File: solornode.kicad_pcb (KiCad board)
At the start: 2 copper layers, 35.9 x 42.4 mm, 77 parts, among them J1 Conn_01x06, Q1 Q_NMOS_GDS, Q4 Q_PNP_BCE, Q5 Q_NPN_BCE, SW1 SW_Push, U1 LM358, U2 OC5864, U3 PY32F003F1xUx, U4 MAX485E, U5 SGM2033-5.0

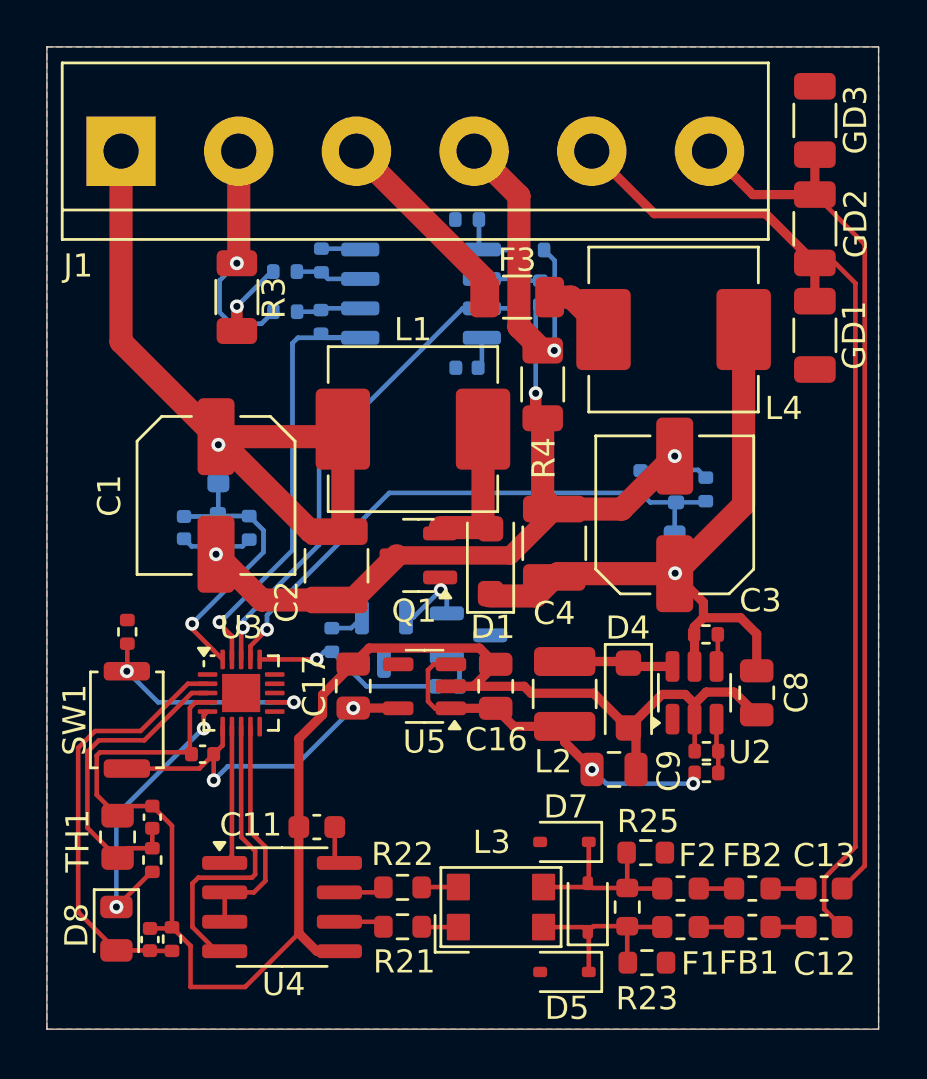
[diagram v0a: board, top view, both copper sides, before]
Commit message: 添加GPIO引出接口和一个LED
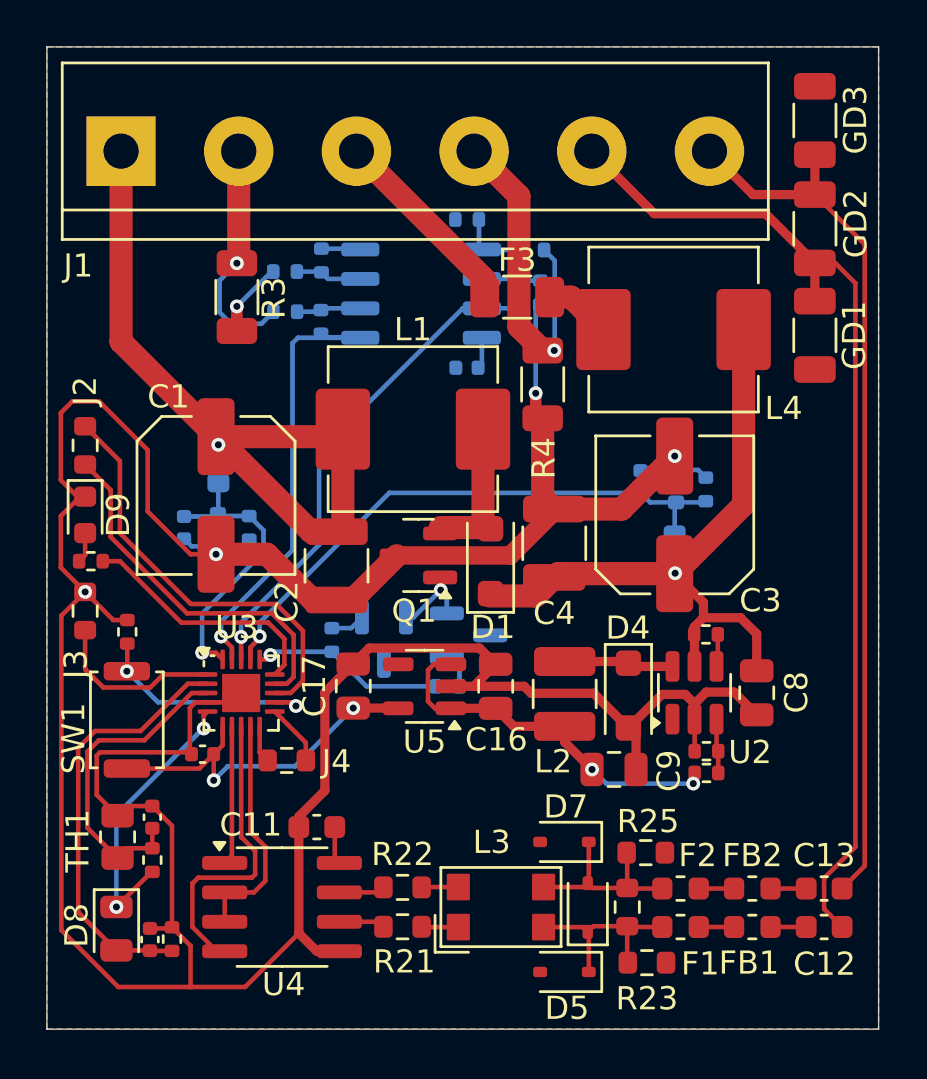
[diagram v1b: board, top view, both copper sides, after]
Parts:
- added D9: LED, LED_SMD:LED_0603_1608Metric, F.Cu at (114.2, 77.1)
- added J2: Conn_01x02, Resistor_SMD:R_0603_1608Metric, F.Cu at (114.2, 74.1)
- added J3: Conn_01x02, Resistor_SMD:R_0603_1608Metric, F.Cu at (114.2, 81.2)
- added J4: Conn_01x02, Resistor_SMD:R_0603_1608Metric, F.Cu at (123.0, 87.7)
- added R28: 470, Resistor_SMD:R_0402_1005Metric, F.Cu at (114.5, 79.1)
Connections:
- U3 pad 1: unconnected-(U3-PA5-Pad1) -> Net-(J3-Pin_1)
- U3 pad 13: unconnected-(U3-OSCIN_PF0-Pad13) -> Net-(J2-Pin_1)
- U3 pad 14: unconnected-(U3-OSCOUT_PF1-Pad14) -> Net-(J2-Pin_2)
- U3 pad 15: unconnected-(U3-NRST_PF2-Pad15) -> Net-(U3-NRST_PF2)
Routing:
- net GND: track 104.6 -> 150.9 mm, vias 2 -> 3
- net Net-(J2-Pin_1): track 0.00 -> 18.5 mm
- net Net-(J2-Pin_2): track 0.00 -> 16.0 mm
- net Net-(U3-NRST_PF2): track 0.00 -> 10.9 mm
- net Net-(J3-Pin_1): track 0.00 -> 7.53 mm
- net /I2C_SDA: track 0.00 -> 2.67 mm
- net /I2C_SCL: track 0.00 -> 1.60 mm
- net Net-(D9-A): track 0.00 -> 1.32 mm

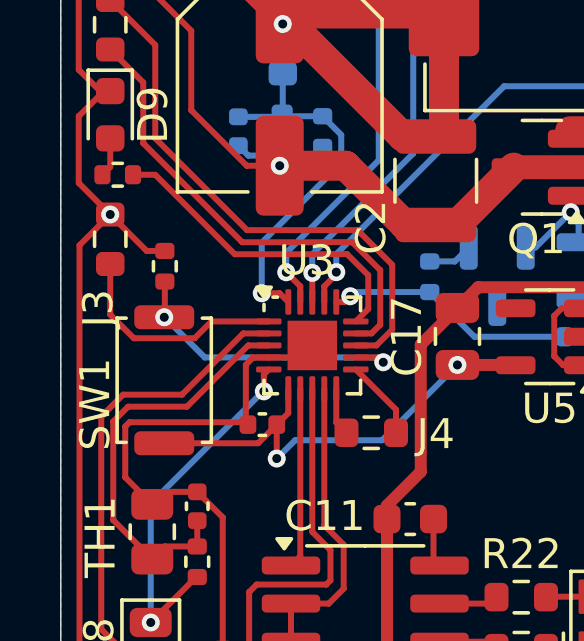
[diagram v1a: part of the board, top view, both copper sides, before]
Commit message: 微调布局和丝印位置
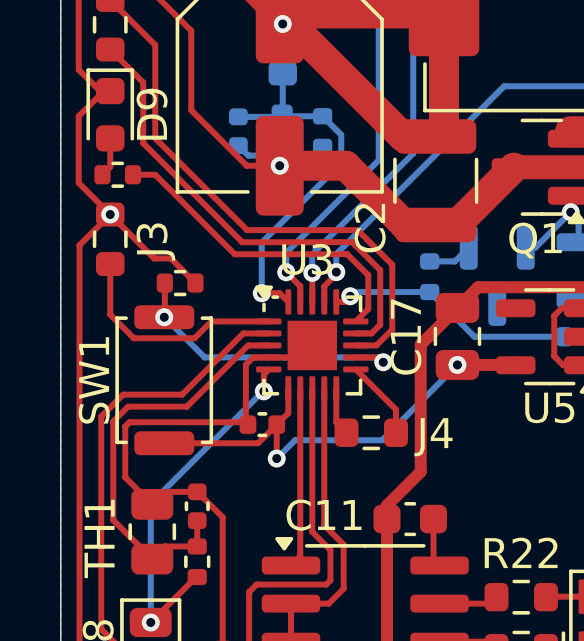
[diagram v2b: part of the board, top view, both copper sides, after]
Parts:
- moved R20 0.76 mm to (116.6, 82.7), turned to 0 degrees
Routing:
- net GND: track 150.9 -> 152.4 mm
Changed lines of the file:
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@@
 	(footprint "Resistor_SMD:R_0402_1005Metric"
 		(layer "F.Cu")
-		(at 116.07 82.15 90)
+		(at 116.58 82.71)
 		(descr "Resistor SMD 0402 (1005 Metric), square (rectangular) end terminal, IPC_7351 nominal, (Body size source: IPC-SM-782 page 72, https://www.pcb-3d.com/wordpress/wp-content/uploads/ipc-sm-782a_amendment_1_and_2.pdf), generated with kicad-footprint-generator")
 		(tags "resistor")
 		(property "Reference" "R20"
-			(at 0 -1.17 90)
+			(at 0 -1.17 360)
 			(layer "F.SilkS")
 			(hide yes)
@@
 		)
 		(property "Value" "R"
-			(at 0 1.17 90)
+			(at 0 1.17 360)
 			(layer "F.Fab")
 			(effects
@@
 		)
 		(property "Footprint" "Resistor_SMD:R_0402_1005Metric"
-			(at 0 0 90)
+			(at 0 0 0)
 			(unlocked yes)
 			(layer "F.Fab")
@@
 		)
 		(property "Datasheet" ""
-			(at 0 0 90)
+			(at 0 0 0)
 			(unlocked yes)
 			(layer "F.Fab")
@@
 		)
 		(property "Description" "Resistor"
-			(at 0 0 90)
+			(at 0 0 0)
 			(unlocked yes)
 			(layer "F.Fab")
@@
 		)
 		(fp_line
-			(start 0.93 -0.47)
-			(end 0.93 0.47)
+			(start -0.93 -0.47)
+			(end 0.93 -0.47)
 			(stroke
 				(width 0.05)
@@
 		)
 		(fp_line
-			(start -0.93 -0.47)
-			(end 0.93 -0.47)
+			(start -0.93 0.47)
+			(end -0.93 -0.47)
 			(stroke
 				(width 0.05)
@@
 		)
 		(fp_line
-			(start 0.93 0.47)
-			(end -0.93 0.47)
+			(start 0.93 -0.47)
+			(end 0.93 0.47)
 			(stroke
 				(width 0.05)
@@
 		)
 		(fp_line
-			(start -0.93 0.47)
-			(end -0.93 -0.47)
+			(start 0.93 0.47)
+			(end -0.93 0.47)
 			(stroke
 				(width 0.05)
@@
 		)
 		(fp_line
-			(start 0.525 -0.27)
-			(end 0.525 0.27)
+			(start -0.525 -0.27)
+			(end 0.525 -0.27)
 			(stroke
 				(width 0.1)
@@
 		)
 		(fp_line
-			(start -0.525 -0.27)
-			(end 0.525 -0.27)
+			(start -0.525 0.27)
+			(end -0.525 -0.27)
 			(stroke
 				(width 0.1)
@@
 		)
 		(fp_line
-			(start 0.525 0.27)
-			(end -0.525 0.27)
+			(start 0.525 -0.27)
+			(end 0.525 0.27)
 			(stroke
 				(width 0.1)
@@
 		)
 		(fp_line
-			(start -0.525 0.27)
-			(end -0.525 -0.27)
+			(start 0.525 0.27)
+			(end -0.525 0.27)
 			(stroke
 				(width 0.1)
@@
 		)
 		(fp_text user "${REFERENCE}"
-			(at 0 0 90)
+			(at 0 0 360)
 			(layer "F.Fab")
 			(effects
@@
 		)
 		(pad "1" smd roundrect
-			(at -0.51 0 90)
+			(at -0.51 0)
 			(size 0.54 0.64)
 			(layers "F.Cu" "F.Paste" "F.Mask")
@@
 		)
 		(pad "2" smd roundrect
-			(at 0.51 0 90)
+			(at 0.51 0)
 			(size 0.54 0.64)
 			(layers "F.Cu" "F.Paste" "F.Mask")
@@
 		(tags "resistor")
 		(property "Reference" "R28"
-			(at 0 -1.17 360)
+			(at 0 -1.17 0)
 			(layer "F.SilkS")
 			(hide yes)
@@
 		)
 		(property "Value" "470"
-			(at 0 1.17 360)
+			(at 0 1.17 0)
 			(layer "F.Fab")
 			(effects
@@
 		)
 		(fp_text user "${REFERENCE}"
-			(at 0 0 360)
+			(at 0 0 0)
 			(layer "F.Fab")
 			(effects
@@
 		(tags "resistor")
 		(property "Reference" "J3"
-			(at -2.3 -0.4 90)
+			(at 0 1.43 90)
 			(layer "F.SilkS")
 			(effects
@@
 		(tags "resistor")
 		(property "Reference" "J4"
-			(at 2.15 0.05 360)
+			(at 2.15 0.05 0)
 			(layer "F.SilkS")
 			(effects
@@
 		)
 		(property "Value" "Conn_01x02"
-			(at 0 1.43 360)
+			(at 0 1.43 0)
 			(layer "F.Fab")
 			(effects
@@
 		)
 		(fp_text user "${REFERENCE}"
-			(at 0 0 360)
+			(at 0 0 0)
 			(layer "F.Fab")
 			(effects
@@
 		(tags "SMD SMT button")
 		(property "Reference" "SW1"
-			(at -0.8 -2.3 90)
+			(at 0.01 -2.3 90)
 			(layer "F.SilkS")
 			(effects
@@
 	)
 	(segment
-		(start 113.2 77.15)
-		(end 114.0375 76.3125)
+		(start 118 90.52)
+		(end 118 94.9025)
 		(width 0.2)
 		(layer "F.Cu")
@@
 	)
 	(segment
-		(start 118 90.52)
-		(end 118 94.9025)
+		(start 114.0375 76.3125)
+		(end 114.25 76.3125)
+		(width 0.2)
+		(layer "F.Cu")
+		(net 1)
+	)
+	(segment
+		(start 117.09 82.71)
+		(end 116.27 81.89)
 		(width 0.2)
 		(layer "F.Cu")
@@
 	)
 	(segment
+		(start 116.27 81.89)
+		(end 115.715 81.89)
+		(width 0.2)
+		(layer "F.Cu")
+		(net 1)
+	)
+	(segment
 		(start 127.7 78.8625)
 		(end 125.7875 80.775)
@@
 	)
 	(segment
+		(start 115.715 81.89)
+		(end 113.2 79.375)
+		(width 0.2)
+		(layer "F.Cu")
+		(net 1)
+	)
+	(segment
 		(start 113.2 75.6)
 		(end 113.2 72.7)
@@
 	)
 	(segment
-		(start 116.07 81.64)
-		(end 115.465 81.64)
+		(start 113.2 77.15)
+		(end 114.0375 76.3125)
 		(width 0.2)
 		(layer "F.Cu")
@@
 	)
 	(segment
-		(start 115.465 81.64)
-		(end 113.2 79.375)
-		(width 0.2)
-		(layer "F.Cu")
-		(net 1)
-	)
-	(segment
-		(start 113.2 79.375)
-		(end 113.2 77.15)
-		(width 0.2)
-		(layer "F.Cu")
-		(net 1)
-	)
-	(segment
 		(start 125.8225 83.54)
 		(end 126.5125 82.85)
@@
 	)
 	(segment
-		(start 114.0375 76.3125)
-		(end 114.25 76.3125)
-		(width 0.2)
-		(layer "F.Cu")
-		(net 1)
-	)
-	(segment
 		(start 123.475 90.125)
 		(end 124.6 89)
@@
 	)
 	(segment
+		(start 113.2 79.375)
+		(end 113.2 77.15)
+		(width 0.2)
+		(layer "F.Cu")
+		(net 1)
+	)
+	(segment
 		(start 118.76 87.35)
 		(end 118.84 87.43)
@@
 	)
 	(segment
-		(start 122.435 85.19)
-		(end 123.19 85.19)
+		(start 116.07 82.71)
+		(end 116.07 83.83)
 		(width 0.2)
 		(layer "F.Cu")
@@
 	)
 	(segment
-		(start 123.19 85.19)
-		(end 123.35 85.35)
+		(start 122.435 85.19)
+		(end 123.19 85.19)
 		(width 0.2)
 		(layer "F.Cu")
@@
 	)
 	(segment
-		(start 116.07 82.66)
-		(end 116.07 83.83)
+		(start 123.19 85.19)
+		(end 123.35 85.35)
 		(width 0.2)
 		(layer "F.Cu")
@@
 	)
 	(group ""
-		(members "09f9c4f3-5e15-4a2a-8be2-e41d80d0421a" "b58a11ee-d392-48e7-b5e6-44345098f280"
-			"e594c711-e0e6-4358-b09f-86c84f6e88f9"
+		(members "09f9c4f3-5e15-4a2a-8be2-e41d80d0421a" "39d7fbea-8246-4baf-88d2-5de6ac0c4fd6"
+			"de4cb7ad-cff2-4c4a-9bbd-0182228d0f14" "e594c711-e0e6-4358-b09f-86c84f6e88f9"
 		)
 	)

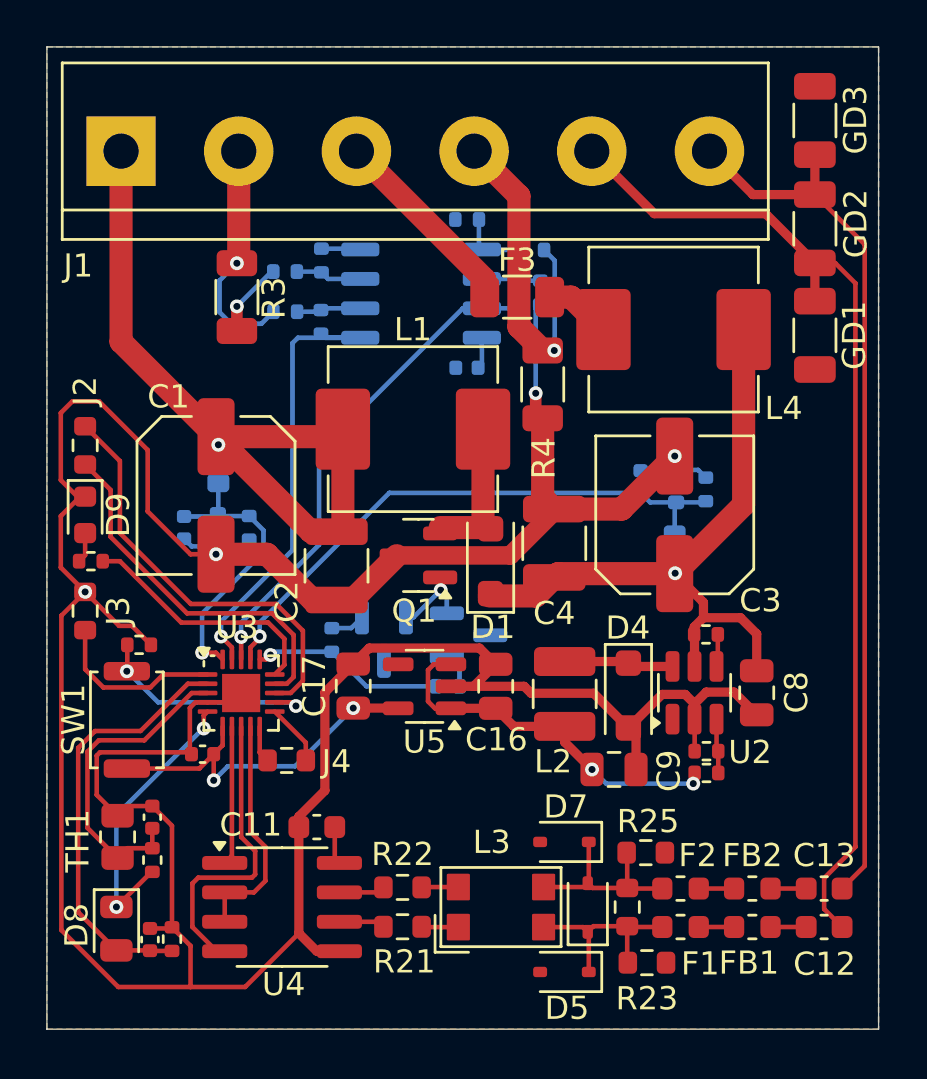
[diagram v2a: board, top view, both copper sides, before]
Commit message: 添加稳压二极管进行电平转换，修改LDO为3.3V，连接5V线路
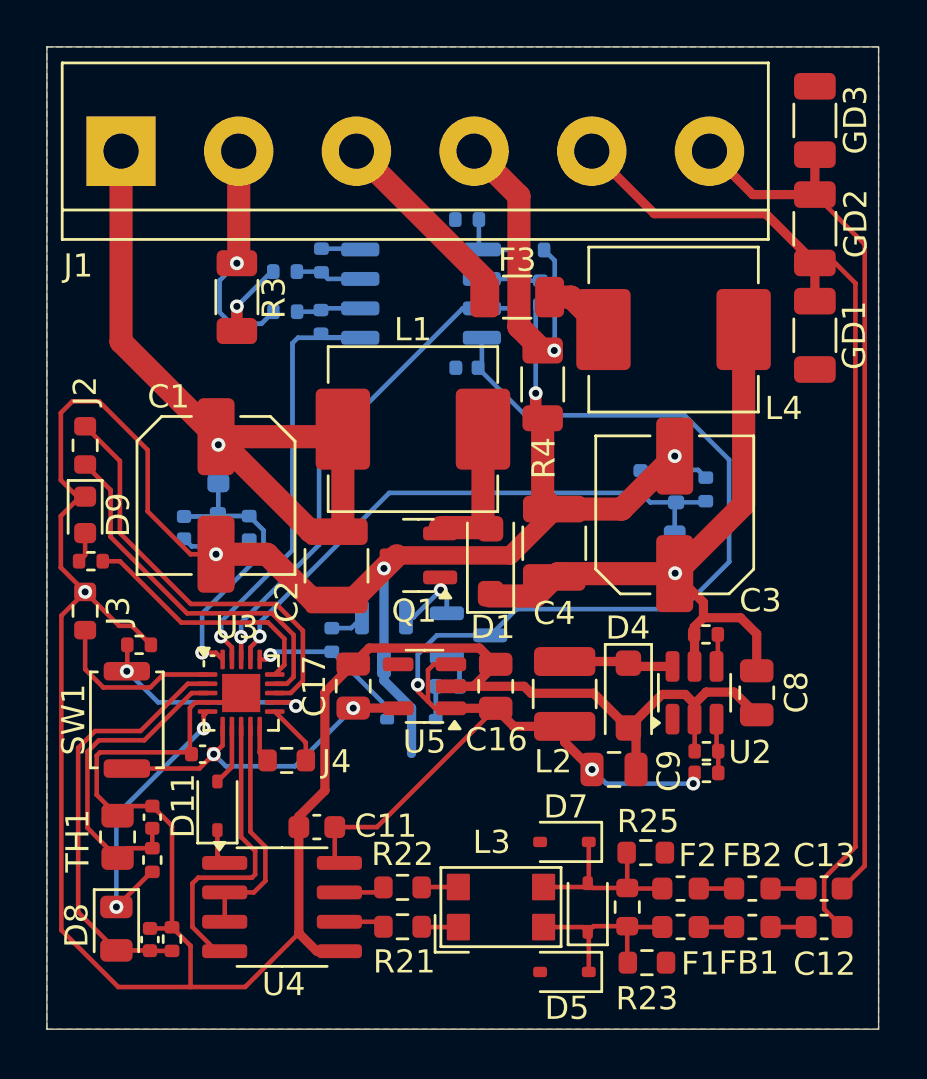
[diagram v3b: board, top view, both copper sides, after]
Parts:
- added D10: 2.0V, Diode_SMD:D_SOD-323, B.Cu at (128.3, 85.9)
- added D11: 2.0V, Diode_SMD:D_SOD-323, F.Cu at (120.0, 89.7)
- R18: value 18k -> 20k
- U5: value SGM2033-5.0 -> SGM2033-3.3
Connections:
- C16 pad 1: /Vdco -> +5V
- C9 pad 1: /Vdco -> +5V
- L2 pad 2: /Vdco -> +5V
- R1 pad 1: /MOS_DrvIn -> Net-(D10-K)
- R19 pad 2: /Vdco -> +5V
- U4 pad 1: /MAX485_RO -> Net-(D11-K)
- U5 pad 1: /Vdco -> +5V
- U5 pad 3: /Vdco -> +5V
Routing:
- net +5V: track 2.99 -> 62.5 mm, vias 0 -> 3
- net /Vdco: track 16.2 -> 0.00 mm, vias 2 -> 0
- net GND: track 152.4 -> 160.9 mm, vias 3 -> 4
- net /MAX485_RO: track 6.01 -> 2.63 mm
- net Net-(D11-K): track 0.00 -> 1.55 mm
- net Net-(D10-K): track 0.00 -> 1.42 mm
- net /MOS_DrvIn: track 8.36 -> 7.15 mm
- net +3.3V: track 15.7 -> 14.6 mm

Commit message: 添加许可证，并在PCB和README.md上添加描述
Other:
- board text added: "SolarNode Photovoltaic Controll yyyy.mm.dd vx.x-gxxxxxxx Copyright (C) 2025 Xu Ruijun License under CERN-OHL-S v2"
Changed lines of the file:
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@@
 		(layer "Edge.Cuts")
+	)
+	(gr_text "SolarNode Photovoltaic Controll\nyyyy.mm.dd vx.x-gxxxxxxx\n\nCopyright (C) 2025 Xu Ruijun\nLicense under CERN-OHL-S v2"
+		(at 142.58 97.14 0)
+		(layer "B.SilkS")
+		(effects
+			(font
+				(size 1 1)
+				(thickness 0.1)
+			)
+			(justify left bottom mirror)
+		)
 	)
 	(segment

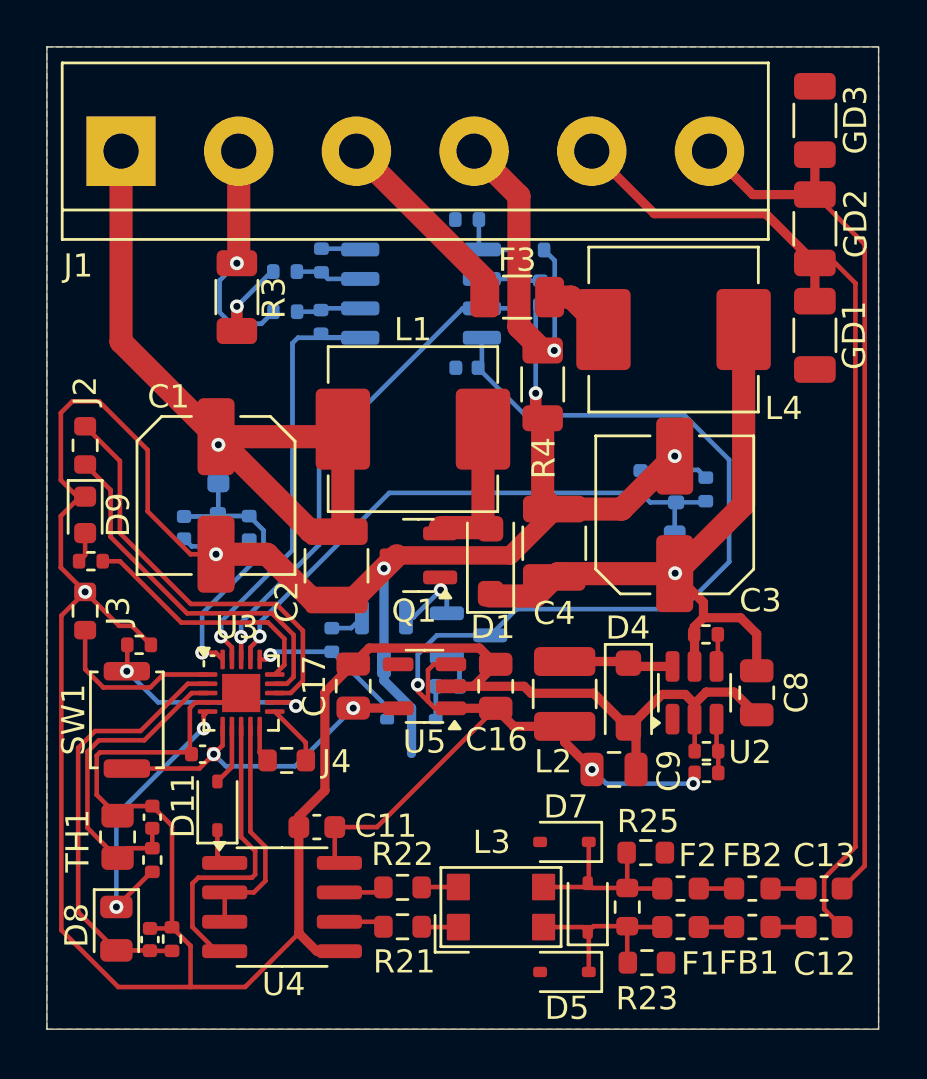
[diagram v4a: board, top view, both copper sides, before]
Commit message: DCDC输入前使用二极管切换电源
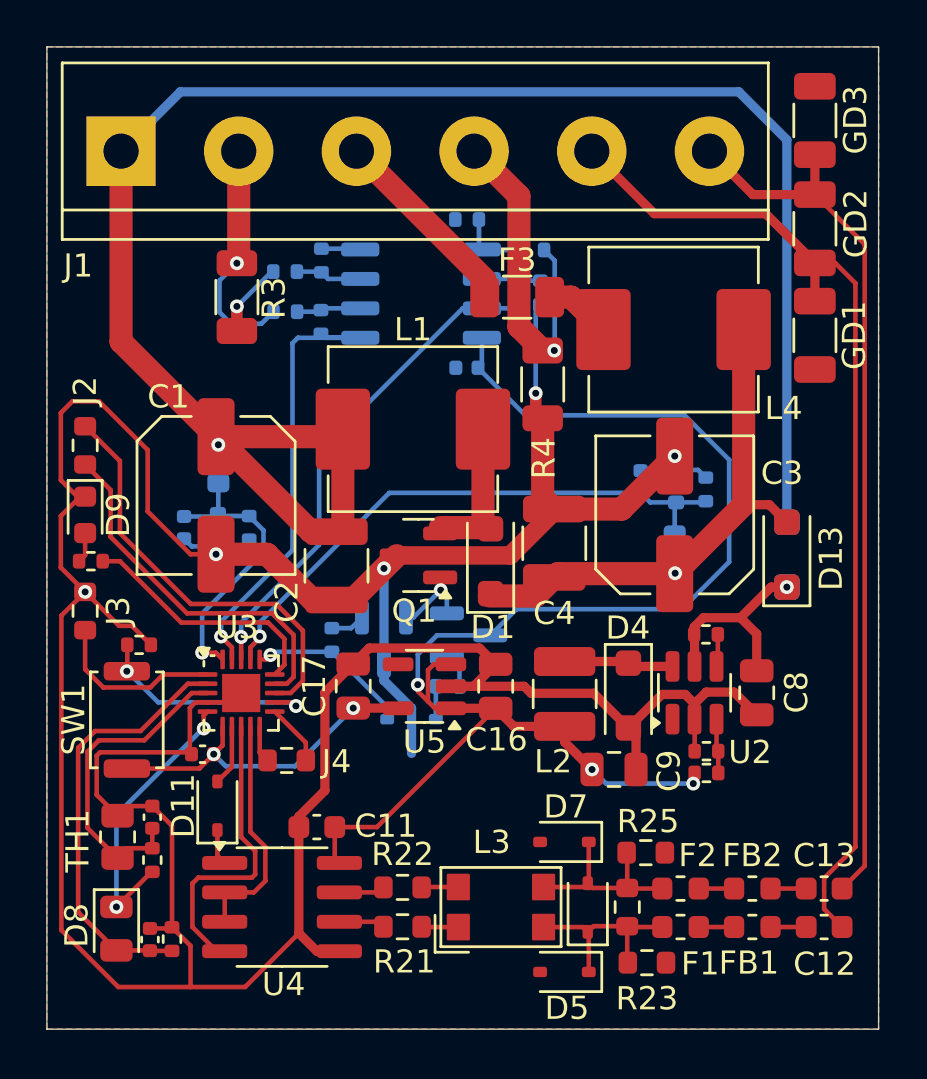
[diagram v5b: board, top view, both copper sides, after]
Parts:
- added D12: D, Diode_SMD:D_SOD-123F, B.Cu at (144.5, 78.8)
- added D13: D, Diode_SMD:D_SOD-123F, F.Cu at (144.5, 78.8)
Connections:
- C3 pad 1: VINP -> /BUS+
- C4 pad 1: VINP -> /BUS+
- D1 pad 1: VINP -> /BUS+
- L4 pad 2: VINP -> /BUS+
- R15 pad 1: VINP -> /BUS+
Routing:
- net /SLR+: track 30.9 -> 78.0 mm
- net /BUS+: track 0.00 -> 22.3 mm, vias 0 -> 1
- net VINP: track 29.0 -> 9.00 mm
